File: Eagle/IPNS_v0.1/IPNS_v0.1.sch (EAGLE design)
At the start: 1 part, among them U1 STM8L152C4_C6TX

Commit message: Powering up microcontroller
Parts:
- added C1, C5, C6, C7, C8, C9: 1u, IPNS_Lib_v0.1:C-USC0805
- added C2, C3: 20pF, IPNS_Lib_v0.1:C-USC0805
- added C4: 100n, IPNS_Lib_v0.1:C-USC0805
- added J1: (no value), IPNS_Lib_v0.1:M04PTH
- added Q1: 16MHz, IPNS_Lib_v0.1:CRYSTALHC49S
- added R1: 0, IPNS_Lib_v0.1:R-US_R0805
- added U$1, U$2: PUSH-BUTTON, IPNS_Lib_v0.1:PUSH-BUTTON
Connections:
- new net +3V3: C1.1, C5.1, C6.1, C7.1, J1.1, U$2.P$1, U1B.VDD, U1B.VDD2, U1B.VLCD
- new net GND: C1.2, C2.1, C3.1, C4.2, C5.2, C6.2, C7.2, C8.2, C9.2, J1.3, U$1.P$1, U1B.VSS1/VSSA/VREF-, U1B.VSS2
- new net N$1: C2.2, Q1.2, U1A.PA2/OSC_IN
- new net N$2: R1.2, U1A.PA3/OSC_OUT
- new net N$5: C3.2, Q1.1, R1.1
- new net RESET: C4.1, J1.4, U$1.P$2, U1A.NRST/PA1
- new net ST_LINK_SWIM: J1.2, U1A.PA0
- new net VDDA: C8.1, C9.1, U$2.P$2, U1B.VDDA, U1B.VREF+
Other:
- note added: "INDUCTOR OR SHORT"

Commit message: Microcontroller setup possibly finished with minor unknowns
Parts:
- added C10, C11: 7pF, IPNS_Lib_v0.1:C-USC0805
- added C12: (no value), IPNS_Lib_v0.1:C-USC0805
- added J2: (no value), IPNS_Lib_v0.1:M04PTH
- added LED1: RED, led:LEDCHIP-LED0805
- added LED2: GREEN, led:LEDCHIP-LED0805
- added LED3: BLUE, led:LEDCHIP-LED0805
- added Q2: 32.768 kHz, IPNS_Lib_v0.1:CRYSTALTC26H
- added R2: 0, IPNS_Lib_v0.1:R-US_R0805
- added R3, R4, R5, R6, R7: (no value), IPNS_Lib_v0.1:R-US_R0805
- C6, C7, C9: value 1u -> 100n
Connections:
- new net DAC: U1A.PF0
- new net N$11: LED1.A, R3.1
- new net N$12: LED2.A, R4.1
- new net N$13: LED3.A, R5.1
- new net N$14: R3.2, U1A.PE7
- new net N$15: R4.2, U1A.PE6
- new net N$16: R5.2, U1A.PE5
- new net N$3: C11.2, Q2.1, R2.1
- new net N$4: C5.1, C6.1, C7.1, U$2.P$1
- new net N$6: C10.2, Q2.2, U1A.PC5/OSC32_IN
- new net N$8: R2.2, U1A.PC6/OSC32_OUT
- new net PULSE: U1A.PD2
- new net SCL: J2.3, R6.1, U1A.PC1
- new net SDA: J2.4, R7.1, U1A.PC0
- net +3V3: now also C12.2, J2.2, R6.2, R7.2; no longer C5.1, C6.1, C7.1, U$2.P$1
- net GND: now also C10.1, C11.1, C12.1, J2.1, LED1.C, LED2.C, LED3.C
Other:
- note added: "C5 and C8 Tantalum?"
- note added: "U2 IS INDUCTOR OR SHORT"
- note removed: "INDUCTOR OR SHORT"
- moved on the sheet: J1

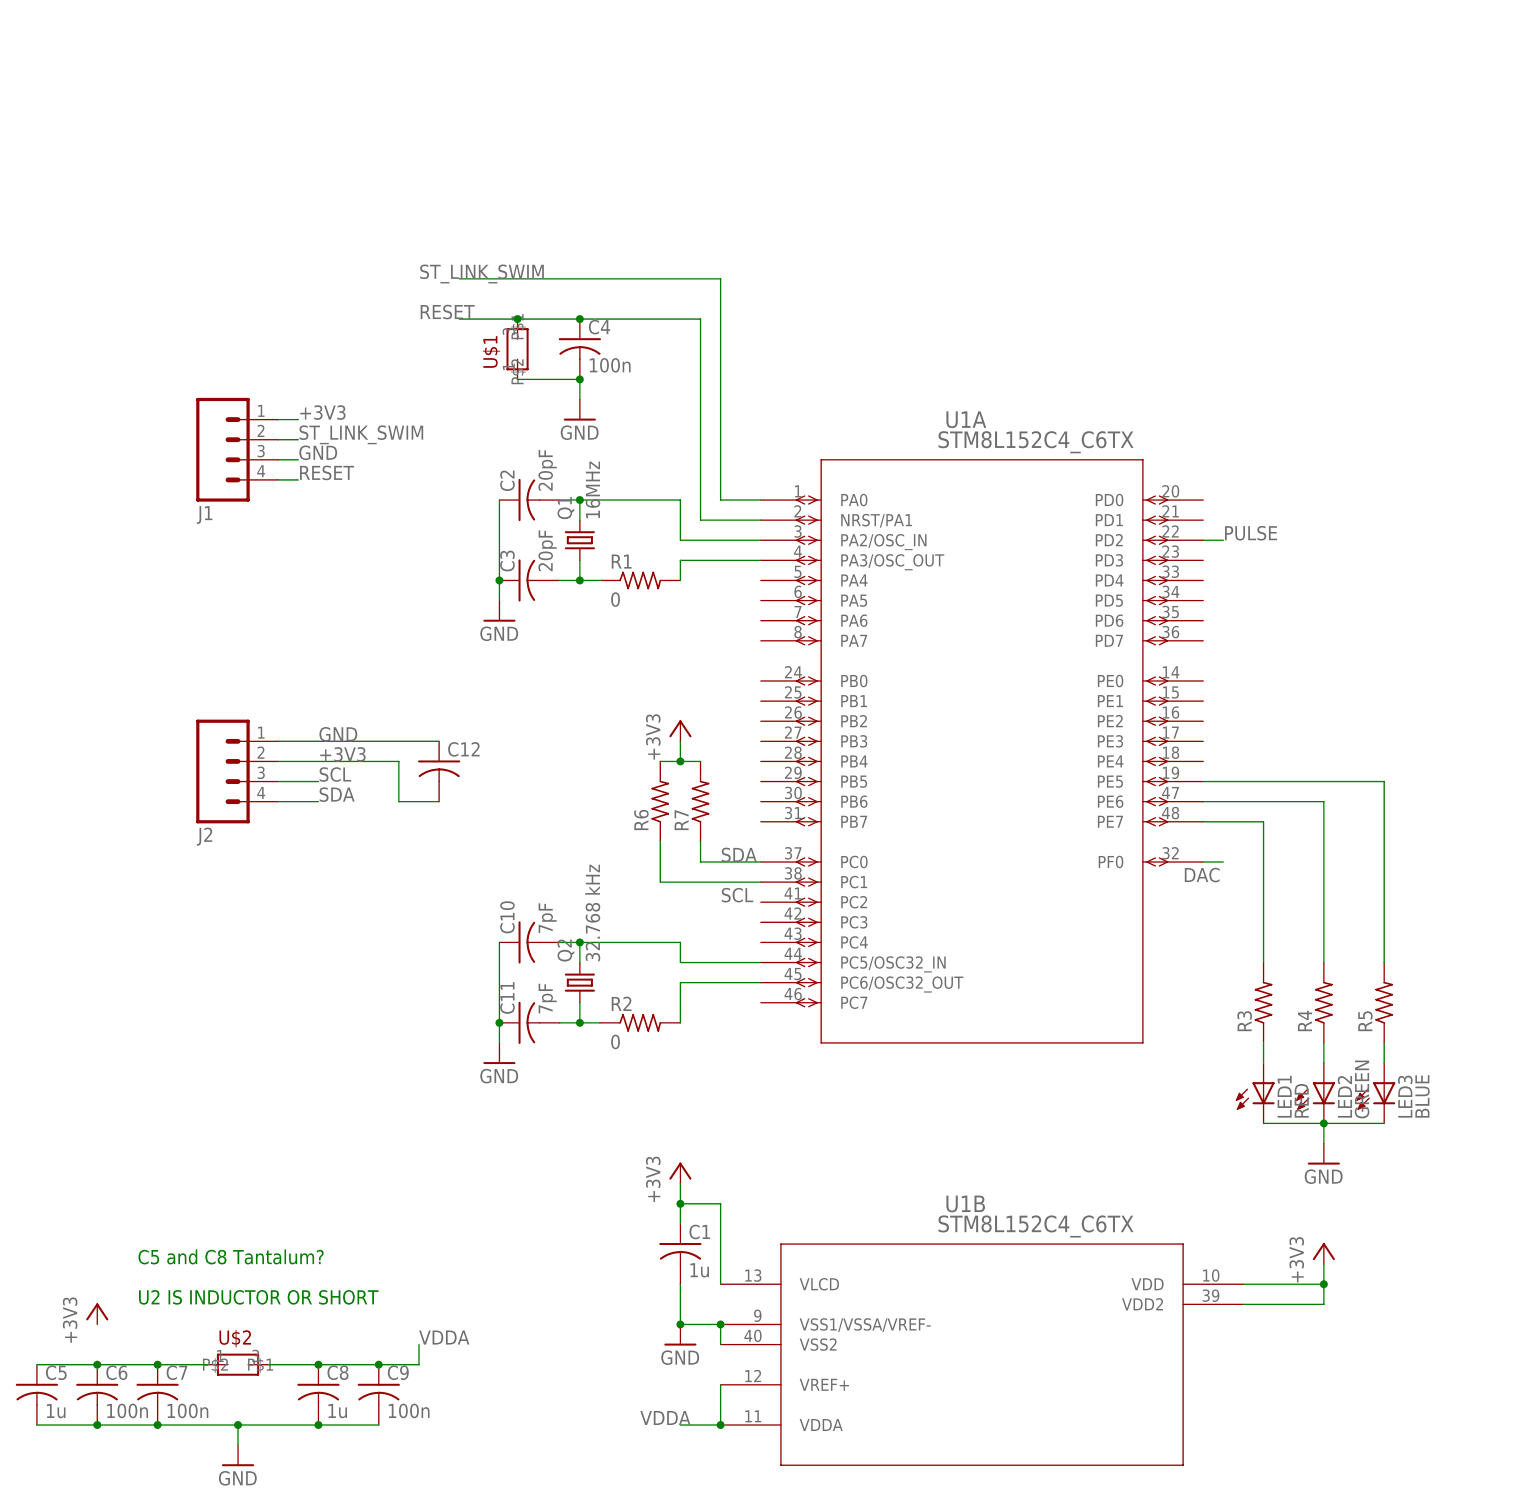
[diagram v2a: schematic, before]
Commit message: Various connectors implemented: SWIM , battery supply board, and NFC memory connector
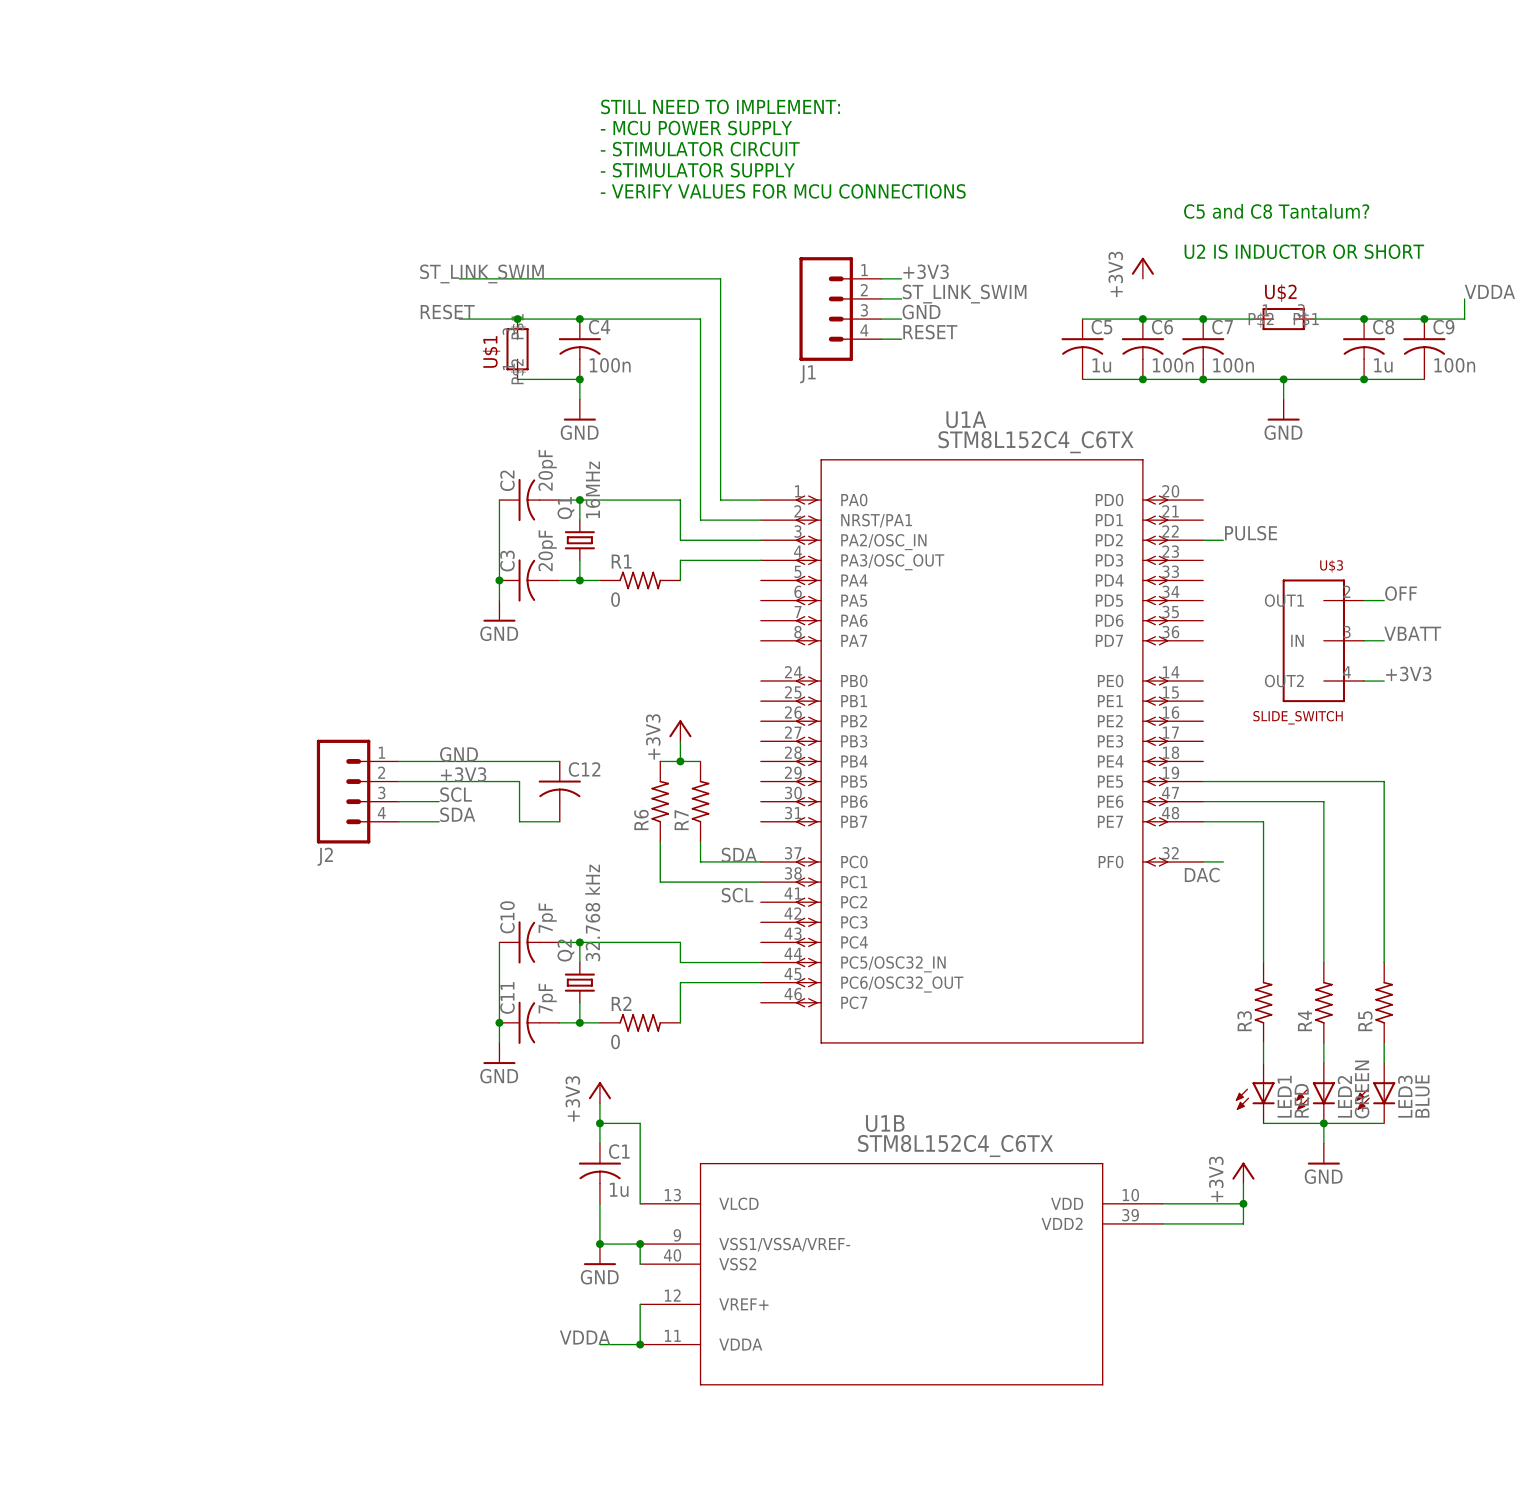
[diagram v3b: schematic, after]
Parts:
- added U$3: SLIDE_SWITCH, IPNS_Lib_v0.1:SLIDE_SWITCH
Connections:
- new net OFF: U$3.OUT1
- new net VBATT: U$3.IN
- net +3V3: now also U$3.OUT2
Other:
- note added: "STILL NEED TO IMPLEMENT: - MCU POWER SUPPLY - STIMULATOR CIRCUIT - STIMULATOR SUPPLY - VERIFY VALUES FOR MCU CONNECTIONS"
- moved on the sheet: C1, C12, C5, C6, C7, C8, C9, J1, J2, U$2, U1B

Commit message: Physical board semi-rearranged
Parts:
- removed R1, R2: 0, IPNS_Lib_v0.1:R-US_R0805
- removed U$2: PUSH-BUTTON, IPNS_Lib_v0.1:PUSH-BUTTON
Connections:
- removed net N$2: R1.2, U1A.PA3/OSC_OUT
- removed net N$4: C5.1, C6.1, C7.1, U$2.P$1
- removed net N$8: R2.2, U1A.PC6/OSC32_OUT
- removed net VDDA: C8.1, C9.1, U$2.P$2, U1B.VDDA, U1B.VREF+
- net +3V3: now also C5.1, C6.1, C7.1, C8.1, C9.1, U1B.VDDA, U1B.VREF+
- net N$14: now also U1A.PE5; no longer U1A.PE7
- net N$15: now also U1A.PE4; no longer U1A.PE6
- net N$16: now also U1A.PE3; no longer U1A.PE5
- net N$3: now also U1A.PC6/OSC32_OUT; no longer R2.1
- net N$5: now also U1A.PA3/OSC_OUT; no longer R1.1
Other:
- moved on the sheet: U$3
